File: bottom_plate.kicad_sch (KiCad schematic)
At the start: 25 parts, among them J42 Osc Out, J43 Conn_02x08_Odd_Even, J44 Conn_02x08_Odd_Even, J45 Conn_02x08_Odd_Even, J46 Conn_02x08_Odd_Even, J47 Conn_02x08_Odd_Even, J48 Select, J49 Select, J60 VCC, J61 VCC, J62 GND, J63 GND, J64 Conn_02x08_Odd_Even, J66 4017 Pins, J67 4017 Pins, J68 Conn_01x18, J73 Conn_02x22_Odd_Even, J74 Conn_02x22_Odd_Even, J75 Conn_02x22_Odd_Even, J76 Conn_02x22_Odd_Even, J77 Conn_02x22_Odd_Even, J78 Conn_02x22_Odd_Even, J79 Conn_02x22_Odd_Even, J80 Conn_02x22_Odd_Even, J81 Conn_02x22_Odd_Even

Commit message: wip symmetric layout
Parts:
- removed J68: Conn_01x18, Connector_PinHeader_2.54mm:PinHeader_1x18_P2.54mm_Vertical, symbol Connector_Generic:Conn_01x18
- removed J73, J74, J75, J76, J77, J78, J79, J80, J81: Conn_02x22_Odd_Even, symbol Connector_Generic:Conn_02x22_Odd_Even
- added J68: Conn_01x16, Connector_PinSocket_2.54mm:PinSocket_1x16_P2.54mm_Vertical, symbol Connector_Generic:Conn_01x16
- added J73, J74, J75, J76, J77, J78, J79, J80, J81, J82: Conn_02x20_Odd_Even, Connector_PinHeader_2.54mm:PinHeader_2x20_P2.54mm_Vertical, symbol Connector_Generic:Conn_02x20_Odd_Even
- added J85, J86: Output, Connector_PinHeader_2.54mm:PinHeader_2x04_P2.54mm_Vertical, symbol Connector_Generic:Conn_02x04_Odd_Even
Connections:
- net 4051 2/X: now also J66.21 (Pin_21), J66.22 (Pin_22)
- net 4051 2/X0: now also J68.9 (Pin_9)
- net 4051 2/X1: now also J68.10 (Pin_10)
- net 4051 2/X2: now also J68.11 (Pin_11)
- net 4051 2/X3: now also J68.12 (Pin_12)
- net 4051 2/X4: now also J68.13 (Pin_13)
- net 4051 2/X5: now also J68.14 (Pin_14)
- net 4051 2/X6: now also J68.15 (Pin_15)
- net 4051 2/X7: now also J68.16 (Pin_16)
- net 4051/X: now also J67.21 (Pin_21), J67.22 (Pin_22)
- net 4051/X0: now also J68.1 (Pin_1)
- net 4051/X1: now also J68.2 (Pin_2)
- net 4051/X2: now also J68.3 (Pin_3)
- net 4051/X3: now also J68.4 (Pin_4)
- net 4051/X4: now also J68.5 (Pin_5)
- net 4051/X5: now also J68.6 (Pin_6)
- net 4051/X6: now also J68.7 (Pin_7)
- net 4051/X7: now also J68.8 (Pin_8)
- net at J66.1 (Pin_1), J66.2 (Pin_2): now also J73.1 (Pin_1), J73.2 (Pin_2), J74.1 (Pin_1), J74.2 (Pin_2), J75.1 (Pin_1), J75.2 (Pin_2), J76.1 (Pin_1), J76.2 (Pin_2), J77.1 (Pin_1), J77.2 (Pin_2), J78.1 (Pin_1), J78.2 (Pin_2), J79.1 (Pin_1), J79.2 (Pin_2), J80.1 (Pin_1), J80.2 (Pin_2), J81.1 (Pin_1), J81.2 (Pin_2), J82.1 (Pin_1), J82.2 (Pin_2)
- net at J66.10 (Pin_10), J66.9 (Pin_9): now also J73.10 (Pin_10), J73.9 (Pin_9), J74.10 (Pin_10), J74.9 (Pin_9), J75.10 (Pin_10), J75.9 (Pin_9), J76.10 (Pin_10), J76.9 (Pin_9), J77.10 (Pin_10), J77.9 (Pin_9), J78.10 (Pin_10), J78.9 (Pin_9), J79.10 (Pin_10), J79.9 (Pin_9), J80.10 (Pin_10), J80.9 (Pin_9), J81.10 (Pin_10), J81.9 (Pin_9), J82.10 (Pin_10), J82.9 (Pin_9)
- net at J66.11 (Pin_11), J66.12 (Pin_12): now also J73.11 (Pin_11), J73.12 (Pin_12), J74.11 (Pin_11), J74.12 (Pin_12), J75.11 (Pin_11), J75.12 (Pin_12), J76.11 (Pin_11), J76.12 (Pin_12), J77.11 (Pin_11), J77.12 (Pin_12), J78.11 (Pin_11), J78.12 (Pin_12), J79.11 (Pin_11), J79.12 (Pin_12), J80.11 (Pin_11), J80.12 (Pin_12), J81.11 (Pin_11), J81.12 (Pin_12), J82.11 (Pin_11), J82.12 (Pin_12)
- net at J66.13 (Pin_13), J66.14 (Pin_14): now also J73.13 (Pin_13), J73.14 (Pin_14), J74.13 (Pin_13), J74.14 (Pin_14), J75.13 (Pin_13), J75.14 (Pin_14), J76.13 (Pin_13), J76.14 (Pin_14), J77.13 (Pin_13), J77.14 (Pin_14), J78.13 (Pin_13), J78.14 (Pin_14), J79.13 (Pin_13), J79.14 (Pin_14), J80.13 (Pin_13), J80.14 (Pin_14), J81.13 (Pin_13), J81.14 (Pin_14), J82.13 (Pin_13), J82.14 (Pin_14)
- net at J66.15 (Pin_15), J66.16 (Pin_16): now also J73.15 (Pin_15), J73.16 (Pin_16), J74.15 (Pin_15), J74.16 (Pin_16), J75.15 (Pin_15), J75.16 (Pin_16), J76.15 (Pin_15), J76.16 (Pin_16), J77.15 (Pin_15), J77.16 (Pin_16), J78.15 (Pin_15), J78.16 (Pin_16), J79.15 (Pin_15), J79.16 (Pin_16), J80.15 (Pin_15), J80.16 (Pin_16), J81.15 (Pin_15), J81.16 (Pin_16), J82.15 (Pin_15), J82.16 (Pin_16)
- net at J66.17 (Pin_17), J66.18 (Pin_18): now also J73.17 (Pin_17), J73.18 (Pin_18), J74.17 (Pin_17), J74.18 (Pin_18), J75.17 (Pin_17), J75.18 (Pin_18), J76.17 (Pin_17), J76.18 (Pin_18), J77.17 (Pin_17), J77.18 (Pin_18), J78.17 (Pin_17), J78.18 (Pin_18), J79.17 (Pin_17), J79.18 (Pin_18), J80.17 (Pin_17), J80.18 (Pin_18), J81.17 (Pin_17), J81.18 (Pin_18), J82.17 (Pin_17), J82.18 (Pin_18)
- net at J66.19 (Pin_19), J66.20 (Pin_20): now also J73.19 (Pin_19), J73.20 (Pin_20), J74.19 (Pin_19), J74.20 (Pin_20), J75.19 (Pin_19), J75.20 (Pin_20), J76.19 (Pin_19), J76.20 (Pin_20), J77.19 (Pin_19), J77.20 (Pin_20), J78.19 (Pin_19), J78.20 (Pin_20), J79.19 (Pin_19), J79.20 (Pin_20), J80.19 (Pin_19), J80.20 (Pin_20), J81.19 (Pin_19), J81.20 (Pin_20), J82.19 (Pin_19), J82.20 (Pin_20)
- net at J67.1 (Pin_1), J67.2 (Pin_2): now also J73.21 (Pin_21), J73.22 (Pin_22), J74.21 (Pin_21), J74.22 (Pin_22), J75.21 (Pin_21), J75.22 (Pin_22), J76.21 (Pin_21), J76.22 (Pin_22), J77.21 (Pin_21), J77.22 (Pin_22), J78.21 (Pin_21), J78.22 (Pin_22), J79.21 (Pin_21), J79.22 (Pin_22), J80.21 (Pin_21), J80.22 (Pin_22), J81.21 (Pin_21), J81.22 (Pin_22), J82.21 (Pin_21), J82.22 (Pin_22)
- net at J67.3 (Pin_3), J67.4 (Pin_4): now also J73.23 (Pin_23), J73.24 (Pin_24), J74.23 (Pin_23), J74.24 (Pin_24), J75.23 (Pin_23), J75.24 (Pin_24), J76.23 (Pin_23), J76.24 (Pin_24), J77.23 (Pin_23), J77.24 (Pin_24), J78.23 (Pin_23), J78.24 (Pin_24), J79.23 (Pin_23), J79.24 (Pin_24), J80.23 (Pin_23), J80.24 (Pin_24), J81.23 (Pin_23), J81.24 (Pin_24), J82.23 (Pin_23), J82.24 (Pin_24)
- net at J67.5 (Pin_5), J67.6 (Pin_6): now also J73.25 (Pin_25), J73.26 (Pin_26), J74.25 (Pin_25), J74.26 (Pin_26), J75.25 (Pin_25), J75.26 (Pin_26), J76.25 (Pin_25), J76.26 (Pin_26), J77.25 (Pin_25), J77.26 (Pin_26), J78.25 (Pin_25), J78.26 (Pin_26), J79.25 (Pin_25), J79.26 (Pin_26), J80.25 (Pin_25), J80.26 (Pin_26), J81.25 (Pin_25), J81.26 (Pin_26), J82.25 (Pin_25), J82.26 (Pin_26)
- net at J67.7 (Pin_7), J67.8 (Pin_8): now also J73.27 (Pin_27), J73.28 (Pin_28), J74.27 (Pin_27), J74.28 (Pin_28), J75.27 (Pin_27), J75.28 (Pin_28), J76.27 (Pin_27), J76.28 (Pin_28), J77.27 (Pin_27), J77.28 (Pin_28), J78.27 (Pin_27), J78.28 (Pin_28), J79.27 (Pin_27), J79.28 (Pin_28), J80.27 (Pin_27), J80.28 (Pin_28), J81.27 (Pin_27), J81.28 (Pin_28), J82.27 (Pin_27), J82.28 (Pin_28)
- net at J66.3 (Pin_3), J66.4 (Pin_4): now also J73.3 (Pin_3), J73.4 (Pin_4), J74.3 (Pin_3), J74.4 (Pin_4), J75.3 (Pin_3), J75.4 (Pin_4), J76.3 (Pin_3), J76.4 (Pin_4), J77.3 (Pin_3), J77.4 (Pin_4), J78.3 (Pin_3), J78.4 (Pin_4), J79.3 (Pin_3), J79.4 (Pin_4), J80.3 (Pin_3), J80.4 (Pin_4), J81.3 (Pin_3), J81.4 (Pin_4), J82.3 (Pin_3), J82.4 (Pin_4)
- net at J67.10 (Pin_10), J67.9 (Pin_9): now also J73.29 (Pin_29), J73.30 (Pin_30), J74.29 (Pin_29), J74.30 (Pin_30), J75.29 (Pin_29), J75.30 (Pin_30), J76.29 (Pin_29), J76.30 (Pin_30), J77.29 (Pin_29), J77.30 (Pin_30), J78.29 (Pin_29), J78.30 (Pin_30), J79.29 (Pin_29), J79.30 (Pin_30), J80.29 (Pin_29), J80.30 (Pin_30), J81.29 (Pin_29), J81.30 (Pin_30), J82.29 (Pin_29), J82.30 (Pin_30)
- net at J67.11 (Pin_11), J67.12 (Pin_12): now also J73.31 (Pin_31), J73.32 (Pin_32), J74.31 (Pin_31), J74.32 (Pin_32), J75.31 (Pin_31), J75.32 (Pin_32), J76.31 (Pin_31), J76.32 (Pin_32), J77.31 (Pin_31), J77.32 (Pin_32), J78.31 (Pin_31), J78.32 (Pin_32), J79.31 (Pin_31), J79.32 (Pin_32), J80.31 (Pin_31), J80.32 (Pin_32), J81.31 (Pin_31), J81.32 (Pin_32), J82.31 (Pin_31), J82.32 (Pin_32)
- net at J67.13 (Pin_13), J67.14 (Pin_14): now also J73.33 (Pin_33), J73.34 (Pin_34), J74.33 (Pin_33), J74.34 (Pin_34), J75.33 (Pin_33), J75.34 (Pin_34), J76.33 (Pin_33), J76.34 (Pin_34), J77.33 (Pin_33), J77.34 (Pin_34), J78.33 (Pin_33), J78.34 (Pin_34), J79.33 (Pin_33), J79.34 (Pin_34), J80.33 (Pin_33), J80.34 (Pin_34), J81.33 (Pin_33), J81.34 (Pin_34), J82.33 (Pin_33), J82.34 (Pin_34)
- net at J67.15 (Pin_15), J67.16 (Pin_16): now also J73.35 (Pin_35), J73.36 (Pin_36), J74.35 (Pin_35), J74.36 (Pin_36), J75.35 (Pin_35), J75.36 (Pin_36), J76.35 (Pin_35), J76.36 (Pin_36), J77.35 (Pin_35), J77.36 (Pin_36), J78.35 (Pin_35), J78.36 (Pin_36), J79.35 (Pin_35), J79.36 (Pin_36), J80.35 (Pin_35), J80.36 (Pin_36), J81.35 (Pin_35), J81.36 (Pin_36), J82.35 (Pin_35), J82.36 (Pin_36)
- net at J67.17 (Pin_17), J67.18 (Pin_18): now also J73.37 (Pin_37), J73.38 (Pin_38), J74.37 (Pin_37), J74.38 (Pin_38), J75.37 (Pin_37), J75.38 (Pin_38), J76.37 (Pin_37), J76.38 (Pin_38), J77.37 (Pin_37), J77.38 (Pin_38), J78.37 (Pin_37), J78.38 (Pin_38), J79.37 (Pin_37), J79.38 (Pin_38), J80.37 (Pin_37), J80.38 (Pin_38), J81.37 (Pin_37), J81.38 (Pin_38), J82.37 (Pin_37), J82.38 (Pin_38)
- net at J67.19 (Pin_19), J67.20 (Pin_20): now also J73.39 (Pin_39), J73.40 (Pin_40), J74.39 (Pin_39), J74.40 (Pin_40), J75.39 (Pin_39), J75.40 (Pin_40), J76.39 (Pin_39), J76.40 (Pin_40), J77.39 (Pin_39), J77.40 (Pin_40), J78.39 (Pin_39), J78.40 (Pin_40), J79.39 (Pin_39), J79.40 (Pin_40), J80.39 (Pin_39), J80.40 (Pin_40), J81.39 (Pin_39), J81.40 (Pin_40), J82.39 (Pin_39), J82.40 (Pin_40)
- net at J66.5 (Pin_5), J66.6 (Pin_6): now also J73.5 (Pin_5), J73.6 (Pin_6), J74.5 (Pin_5), J74.6 (Pin_6), J75.5 (Pin_5), J75.6 (Pin_6), J76.5 (Pin_5), J76.6 (Pin_6), J77.5 (Pin_5), J77.6 (Pin_6), J78.5 (Pin_5), J78.6 (Pin_6), J79.5 (Pin_5), J79.6 (Pin_6), J80.5 (Pin_5), J80.6 (Pin_6), J81.5 (Pin_5), J81.6 (Pin_6), J82.5 (Pin_5), J82.6 (Pin_6)
- net at J66.7 (Pin_7), J66.8 (Pin_8): now also J73.7 (Pin_7), J73.8 (Pin_8), J74.7 (Pin_7), J74.8 (Pin_8), J75.7 (Pin_7), J75.8 (Pin_8), J76.7 (Pin_7), J76.8 (Pin_8), J77.7 (Pin_7), J77.8 (Pin_8), J78.7 (Pin_7), J78.8 (Pin_8), J79.7 (Pin_7), J79.8 (Pin_8), J80.7 (Pin_7), J80.8 (Pin_8), J81.7 (Pin_7), J81.8 (Pin_8), J82.7 (Pin_7), J82.8 (Pin_8)
- new net: J86.1 (Pin_1), J86.2 (Pin_2)
- new net: J86.3 (Pin_3), J86.4 (Pin_4)
- new net: J86.5 (Pin_5), J86.6 (Pin_6)
- new net: J86.7 (Pin_7), J86.8 (Pin_8)
- new net: J85.1 (Pin_1), J85.2 (Pin_2)
- new net: J85.3 (Pin_3), J85.4 (Pin_4)
- new net: J85.5 (Pin_5), J85.6 (Pin_6)
- new net: J85.7 (Pin_7), J85.8 (Pin_8)
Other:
- note added: "18x20 Matrix"
- note added: "Passtrough"
- note removed: "18x22 Matrix"
- moved on the sheet: J60, J61, J62, J63, J66, J67

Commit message: wip assemblying everything 2
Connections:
- net at J73.21 (Pin_21), J73.22 (Pin_22), J74.21 (Pin_21)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: now also J67.19 (Pin_19), J67.20 (Pin_20); no longer J67.1 (Pin_1), J67.2 (Pin_2)
- net at J73.29 (Pin_29), J73.30 (Pin_30), J74.29 (Pin_29)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: now also J67.11 (Pin_11), J67.12 (Pin_12); no longer J67.10 (Pin_10), J67.9 (Pin_9)
- net at J73.31 (Pin_31), J73.32 (Pin_32), J74.31 (Pin_31)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: now also J67.10 (Pin_10), J67.9 (Pin_9); no longer J67.11 (Pin_11), J67.12 (Pin_12)
- net at J73.33 (Pin_33), J73.34 (Pin_34), J74.33 (Pin_33)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: now also J67.7 (Pin_7), J67.8 (Pin_8); no longer J67.13 (Pin_13), J67.14 (Pin_14)
- net at J73.35 (Pin_35), J73.36 (Pin_36), J74.35 (Pin_35)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: now also J67.5 (Pin_5), J67.6 (Pin_6); no longer J67.15 (Pin_15), J67.16 (Pin_16)
- net at J73.37 (Pin_37), J73.38 (Pin_38), J74.37 (Pin_37)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: now also J67.3 (Pin_3), J67.4 (Pin_4); no longer J67.17 (Pin_17), J67.18 (Pin_18)
- net at J73.40 (Pin_40), J74.39 (Pin_39), J74.40 (Pin_40)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: no longer J67.19 (Pin_19), J67.20 (Pin_20), J73.39 (Pin_39)
- net at J73.23 (Pin_23), J73.24 (Pin_24), J74.23 (Pin_23)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: now also J67.17 (Pin_17), J67.18 (Pin_18); no longer J67.3 (Pin_3), J67.4 (Pin_4)
- net at J73.25 (Pin_25), J73.26 (Pin_26), J74.25 (Pin_25)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: now also J67.15 (Pin_15), J67.16 (Pin_16); no longer J67.5 (Pin_5), J67.6 (Pin_6)
- net at J73.27 (Pin_27), J73.28 (Pin_28), J74.27 (Pin_27)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: now also J67.13 (Pin_13), J67.14 (Pin_14); no longer J67.7 (Pin_7), J67.8 (Pin_8)
- net GND2: now reaches J62.1 (Pin_1), J62.2 (Pin_2), J63.1 (Pin_1), J63.2 (Pin_2)
- net VDDF: now reaches J60.1 (Pin_1), J60.2 (Pin_2), J61.1 (Pin_1), J61.2 (Pin_2)
- new net: J67.1 (Pin_1), J67.2 (Pin_2), J73.39 (Pin_39)
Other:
- moved on the sheet: J42

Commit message: 3 board alignment
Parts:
- removed J82: Conn_02x20_Odd_Even, Connector_PinHeader_2.54mm:PinHeader_2x20_P2.54mm_Vertical, symbol Connector_Generic:Conn_02x20_Odd_Even
- added J87: AudioJack3, Connector_Audio:Jack_3.5mm_CUI_SJ1-3523N_Horizontal, symbol Connector_Audio:AudioJack3
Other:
- note added: "16x20 Matrix"
- note removed: "18x20 Matrix"

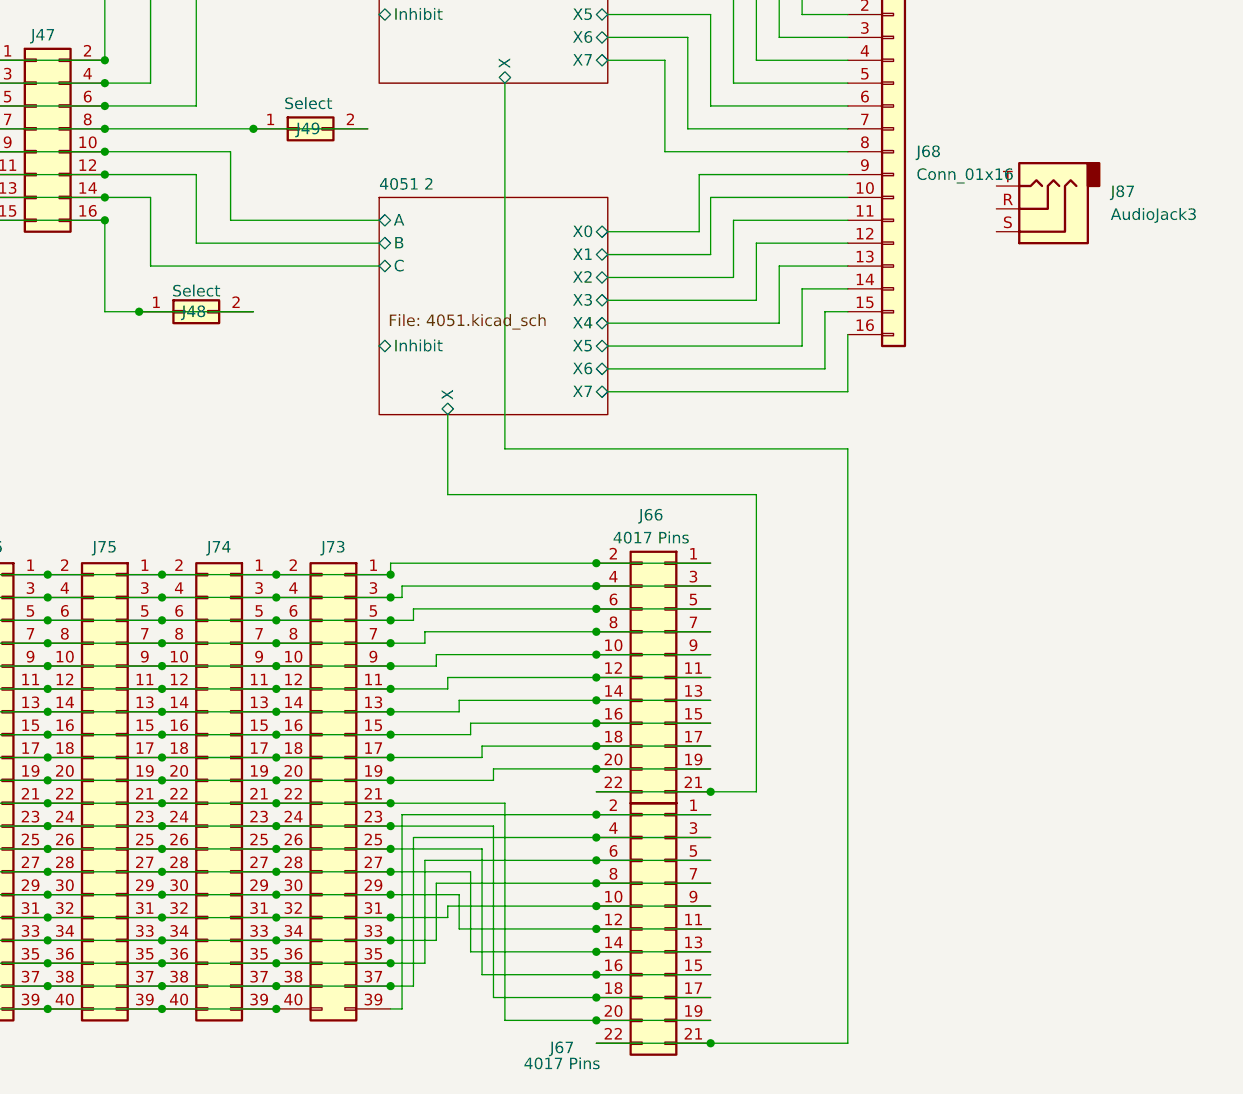
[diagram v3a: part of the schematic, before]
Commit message: bottom plate routed
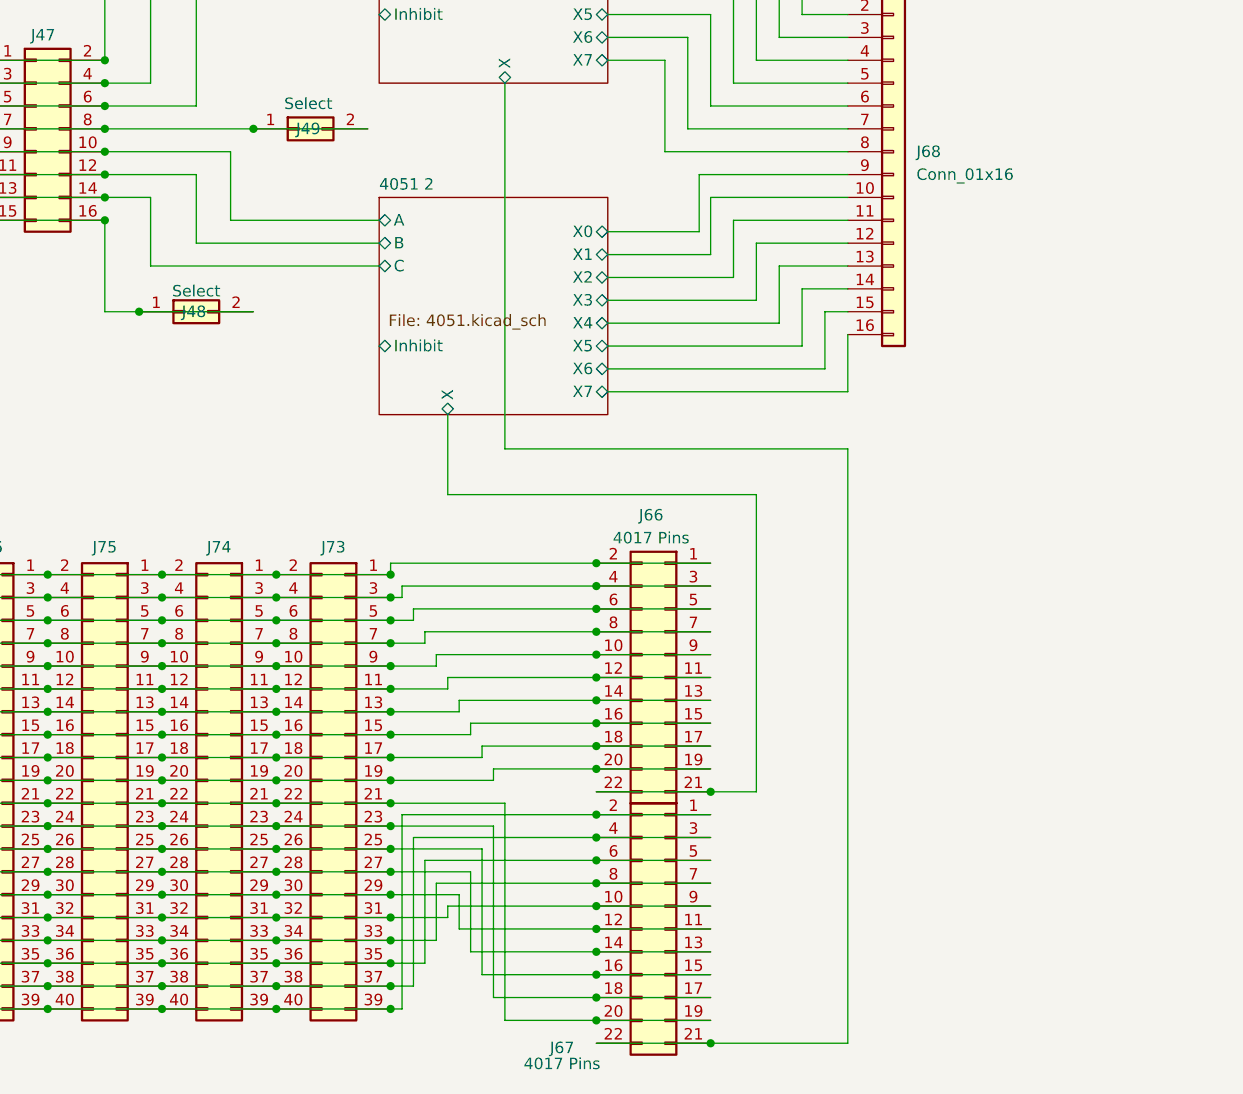
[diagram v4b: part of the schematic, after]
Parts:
- removed J87: AudioJack3, Connector_Audio:Jack_3.5mm_CUI_SJ1-3523N_Horizontal, symbol Connector_Audio:AudioJack3
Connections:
- net at J67.1 (Pin_1), J67.2 (Pin_2), J73.39 (Pin_39): now also J73.40 (Pin_40), J74.39 (Pin_39), J74.40 (Pin_40), J75.39 (Pin_39), J75.40 (Pin_40), J76.39 (Pin_39), J76.40 (Pin_40), J77.39 (Pin_39), J77.40 (Pin_40), J78.39 (Pin_39), J78.40 (Pin_40), J79.39 (Pin_39), J79.40 (Pin_40), J80.39 (Pin_39), J80.40 (Pin_40), J81.39 (Pin_39), J81.40 (Pin_40)
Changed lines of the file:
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@@
 	)
 	(junction
+		(at 186.69 157.48)
+		(diameter 0)
+		(color 0 0 0 0)
+	)
+	(junction
 		(at 154.94 67.31)
 		(diameter 0)
@@
 	)
 	(junction
+		(at 199.39 157.48)
+		(diameter 0)
+		(color 0 0 0 0)
+	)
+	(junction
 		(at 167.64 52.07)
 		(diameter 0)
@@
 	)
 	(junction
-		(at 186.69 157.48)
-		(diameter 0)
-		(color 0 0 0 0)
-	)
-	(junction
 		(at 222.25 138.43)
 		(diameter 0)
@@
 	(wire
 		(pts
+			(xy 222.25 135.89) (xy 234.95 135.89)
+		)
+		(stroke
+			(width 0)
+			(type default)
+		)
+	)
+	(wire
+		(pts
 			(xy 135.89 147.32) (xy 148.59 147.32)
 		)
@@
 	(wire
 		(pts
+			(xy 186.69 157.48) (xy 199.39 157.48)
+		)
+		(stroke
+			(width 0)
+			(type default)
+		)
+	)
+	(wire
+		(pts
 			(xy 116.84 54.61) (xy 129.54 54.61)
 		)
@@
 	(wire
 		(pts
-			(xy 186.69 157.48) (xy 173.99 157.48)
-		)
-		(stroke
-			(width 0)
-			(type default)
-		)
-	)
-	(wire
-		(pts
 			(xy 204.47 119.38) (xy 199.39 119.38)
 		)
@@
 	(wire
 		(pts
+			(xy 173.99 157.48) (xy 186.69 157.48)
+		)
+		(stroke
+			(width 0)
+			(type default)
+		)
+	)
+	(wire
+		(pts
 			(xy 186.69 152.4) (xy 199.39 152.4)
 		)
@@
 	(wire
 		(pts
+			(xy 199.39 157.48) (xy 200.66 157.48)
+		)
+		(stroke
+			(width 0)
+			(type default)
+		)
+	)
+	(wire
+		(pts
 			(xy 234.95 138.43) (xy 222.25 138.43)
 		)
@@
 	(wire
 		(pts
-			(xy 199.39 157.48) (xy 200.66 157.48)
-		)
-		(stroke
-			(width 0)
-			(type default)
-		)
-	)
-	(wire
-		(pts
 			(xy 186.69 116.84) (xy 199.39 116.84)
 		)
@@
 	(wire
 		(pts
-			(xy 234.95 135.89) (xy 222.25 135.89)
-		)
-		(stroke
-			(width 0)
-			(type default)
-		)
-	)
-	(wire
-		(pts
 			(xy 111.76 154.94) (xy 113.03 154.94)
 		)
@@
 					(unit 1)
 				)
-			)
-		)
-	)
-	(symbol
-		(lib_id "Connector_Audio:AudioJack3")
-		(at 271.78 68.58 180)
-		(unit 1)
-		(exclude_from_sim no)
-		(in_bom yes)
-		(on_board yes)
-		(dnp no)
-		(fields_autoplaced yes)
-		(property "Reference" "J87"
-			(at 279.4 66.6749 0)
-			(effects
-				(font
-					(size 1.27 1.27)
-				)
-				(justify right)
-			)
-		)
-		(property "Value" "AudioJack3"
-			(at 279.4 69.2149 0)
-			(effects
-				(font
-					(size 1.27 1.27)
-				)
-				(justify right)
-			)
-		)
-		(property "Footprint" "Connector_Audio:Jack_3.5mm_CUI_SJ1-3523N_Horizontal"
-			(at 271.78 68.58 0)
-			(effects
-				(font
-					(size 1.27 1.27)
-				)
-				(hide yes)
-			)
-		)
-		(property "Datasheet" "~"
-			(at 271.78 68.58 0)
-			(effects
-				(font
-					(size 1.27 1.27)
-				)
-				(hide yes)
-			)
-		)
-		(property "Description" "Audio Jack, 3 Poles (Stereo / TRS)"
-			(at 271.78 68.58 0)
-			(effects
-				(font
-					(size 1.27 1.27)
-				)
-				(hide yes)
-			)
-		)
-		(pin "S"
-		)
-		(pin "R"
-		)
-		(pin "T"
-		)
-		(instances
-			(project ""
-				(path "/01c1f2c1-4d06-4880-847a-9ab55552e3fd/44f3fb3f-0223-4473-937a-c9802bdd1286"
-					(reference "J87")
-					(unit 1)
-				)
-				(path "/01c1f2c1-4d06-4880-847a-9ab55552e3fd/f24cd694-7269-45a2-849b-37748504d3d5"
-					(reference "J87")
-					(unit 1)
-				)

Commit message: 18x20 design
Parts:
- removed J68: Conn_01x16, Connector_PinSocket_2.54mm:PinSocket_1x16_P2.54mm_Vertical, symbol Connector_Generic:Conn_01x16
- added J88: Conn_01x18, Connector_PinHeader_2.54mm:PinHeader_1x18_P2.54mm_Vertical, symbol Connector_Generic:Conn_01x18
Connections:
- net 4051 2/Inhibit: now also J88.18 (Pin_18)
- net 4051 2/X0: now also J88.9 (Pin_9)
- net 4051 2/X1: now also J88.10 (Pin_10)
- net 4051 2/X2: now also J88.11 (Pin_11)
- net 4051 2/X3: now also J88.12 (Pin_12)
- net 4051 2/X4: now also J88.13 (Pin_13)
- net 4051 2/X5: now also J88.14 (Pin_14)
- net 4051 2/X6: now also J88.15 (Pin_15)
- net 4051 2/X7: now also J88.16 (Pin_16)
- net 4051/Inhibit: now also J88.17 (Pin_17)
- net 4051/X0: now also J88.1 (Pin_1)
- net 4051/X1: now also J88.2 (Pin_2)
- net 4051/X2: now also J88.3 (Pin_3)
- net 4051/X3: now also J88.4 (Pin_4)
- net 4051/X4: now also J88.5 (Pin_5)
- net 4051/X5: now also J88.6 (Pin_6)
- net 4051/X6: now also J88.7 (Pin_7)
- net 4051/X7: now also J88.8 (Pin_8)
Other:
- moved on the sheet: J49
